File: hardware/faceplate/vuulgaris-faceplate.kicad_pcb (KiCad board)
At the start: 4 copper layers, 298.3 x 137.8 mm, 54 parts, among them J1 HX JN2.54-2x5P TP H8.9, U1 MSP430FR2675TPT, Y1 32.768kHz FC-135 12.5pF

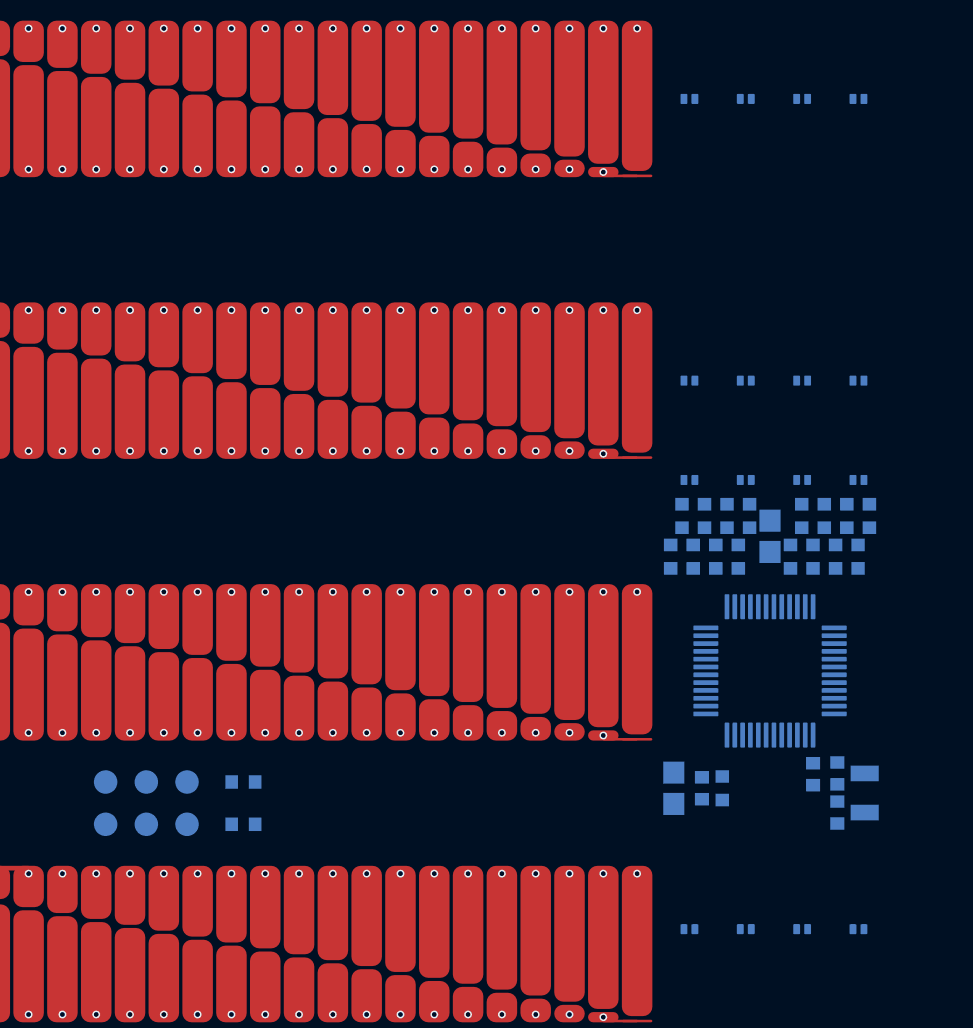
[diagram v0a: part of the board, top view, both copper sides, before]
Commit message: faceplate: networks as a 4x4 grid, silk that does not collide
Dylan: the resistor block did not look good. It was two rows interleaved
at 0.72mm, so the silk boxes overlapped, and the TVS rows (RX0-RX3 per
pad) did not match the R order (block-major), so the ratsnest crossed.

Now one column per CapTIvate block, standing over its own pins, and one
row per pad. Each cell is the TVS directly on its 470R, pin 1 over pin 1
(ADR 0004 already puts both by the MCU; what counts is the order and a
short ground). Traces run down the left of every column: worked through
both corners, that order reaches pins 23-39 with no crossing, so every
TVS grounds to its right and all 16 cells are the same. C3 sits in the
wider middle channel over pin 31.

Pitches from the silk, not the library's undersized courtyards: rows 4.0,
columns 3.2 / 4.5 / 3.2. The crystal group respaced (C2 across the corner
by pins 1/48, C5/C6 lying beside Y1's pads); test pads in one row with
signal labels on silk, per the main board's rule; 470R references on end
beside each part, TVS and TP references on B.Fab. Silk overlaps 61 -> 0;
the 31 silk-over-copper left are the library's pin-1 dots, as on the
main board.

Checked: mksch/netcheck 145/145; boardcheck parity 0, clearance 0; DRC
--unrouted 0 errors; panelcheck 10 OK, 1 TODO (OLED window).
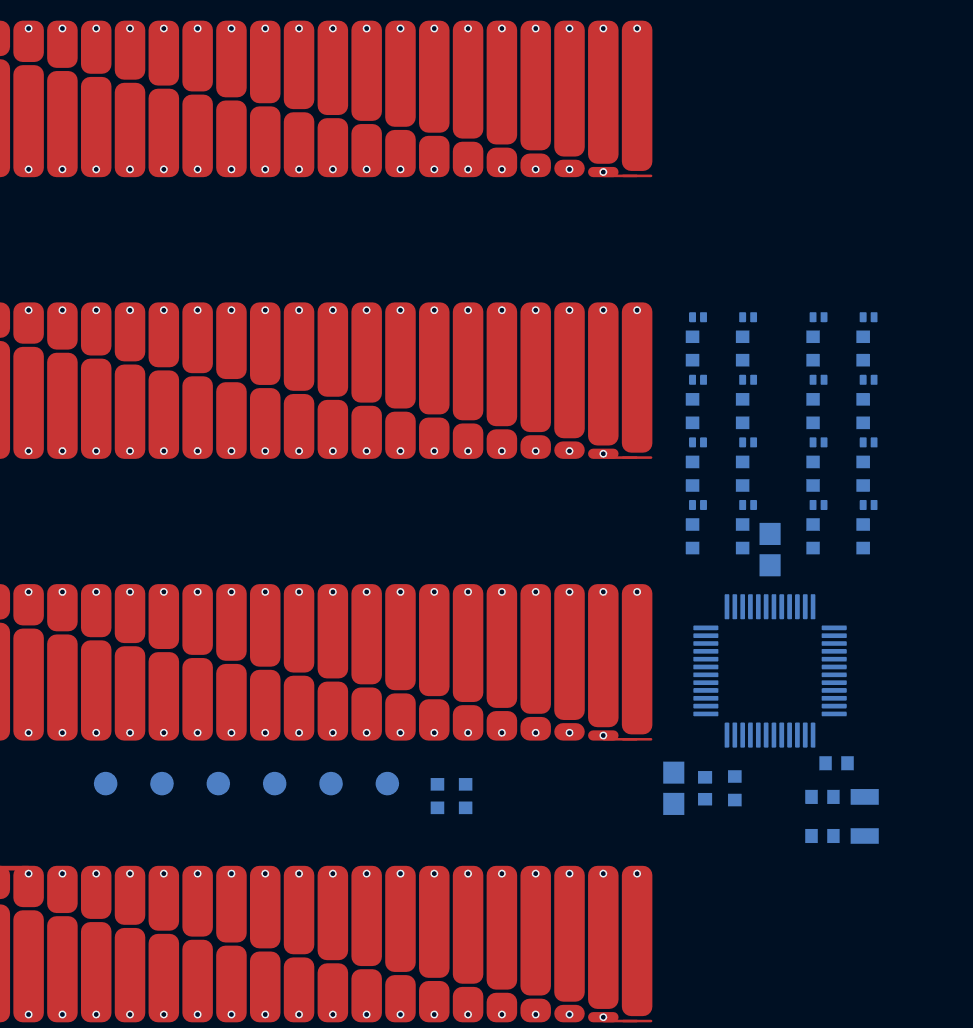
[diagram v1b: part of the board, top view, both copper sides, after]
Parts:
- moved D43 27.1 mm to (387.6, 143.4)
- moved D44 27.1 mm to (390.8, 143.4)
- moved D41 27.1 mm to (379.9, 143.4)
- moved D42 27.1 mm to (383.1, 143.4)
- moved R3 14.3 mm to (365.0, 162.0), turned to -90 degrees
- moved D13 14.0 mm to (387.6, 131.4)
- moved D14 14.0 mm to (390.8, 131.4)
- moved D11 14.0 mm to (379.9, 131.4)
- moved D12 13.9 mm to (383.1, 131.4)
- moved R14 13.4 mm to (390.4, 133.4)
- moved R12 13.4 mm to (382.7, 133.4)
- moved R13 13.4 mm to (387.2, 133.4)
- moved R11 13.4 mm to (379.5, 133.4)
- moved TP6 13.1 mm to (360.0, 161.2)
- moved R2 12.4 mm to (363.2, 162.0), turned to -90 degrees
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
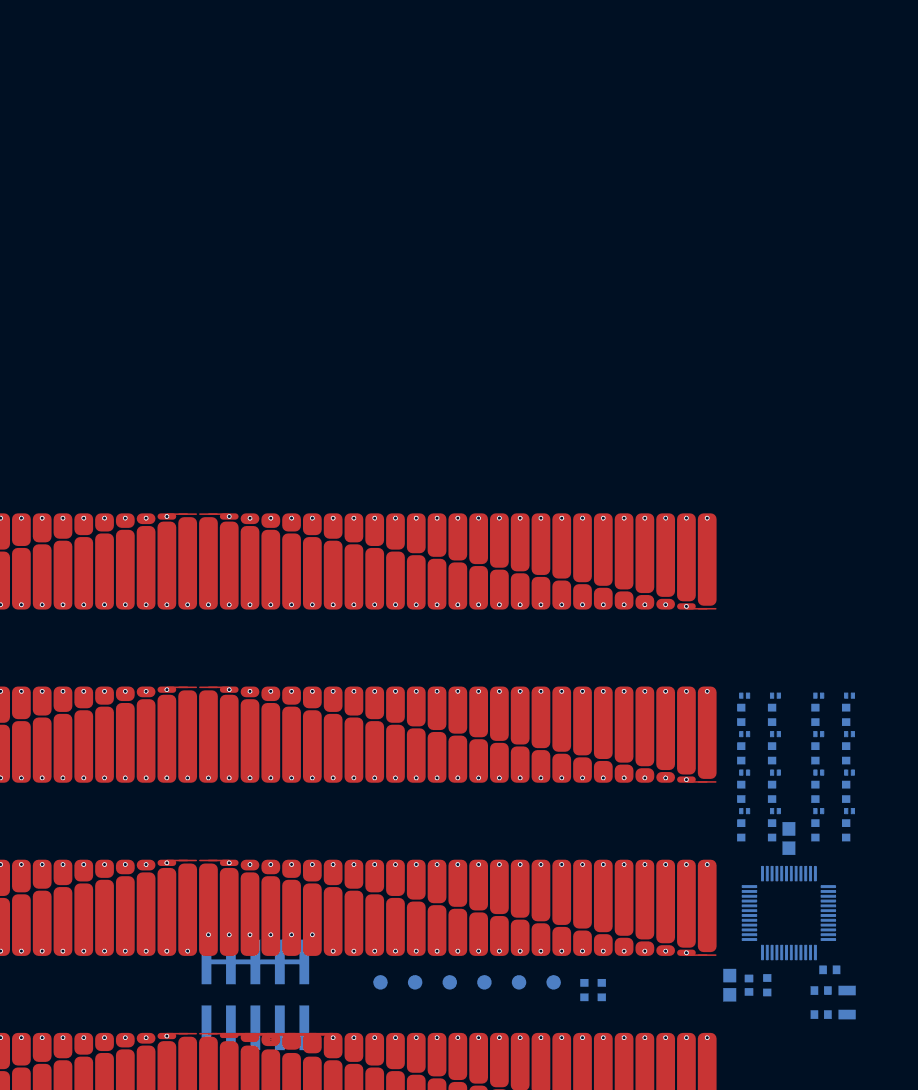
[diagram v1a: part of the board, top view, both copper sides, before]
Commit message: faceplate: OLED window; a wall check that caught parts on the wall top
The window is derived, not drawn: the generator's oled_window() takes the
DS1 position it already emits, the HS242L01 drawing (PCB 72 x 43 -- the
spec table's "68 x 43" is the hole pitch -- AA 55.01 x 27.49 centred
along the long axis, 5.11 below the top edge and 10.4 above the bottom)
and the stack-up. The lift is not chosen (3-5mm), so it is sized at the
deepest: face 4.4mm under the outer surface. 60.09 x 33.90, r 1.0: the
whole active area in view at 45 deg from the player's side, 30 from the
sides, 25 from the back, and never within 1mm of the glass edge, so only
black glass shows past the pixels. It is lopsided because the glass's
wide black band is on the player's side. The panel art draws the window
in place of the old 70 x 42 stand-in box. No chamfer: JLC cannot bevel
an internal cutout.

mkholes.py draws it on Edge.Cuts; panelcheck checks it against the
generator, and the generator's module centre against the main board's
four DS1 holes (both watched failing on a 0.2mm plant). panelcheck
--strict: 13 OK, 0 TODO.

Also a new panelcheck row: every back-side part inside the enclosure
walls, where the faceplate rests on the wall tops. It caught Dylan's
Pcbnew adjustments (grid +1.25/-0.25, corner group lowered, saved 03:43)
putting D14/D24/D34/D44 and Y1 0.56-0.64mm onto the wall; it passes on
the previous commit. Kept his moves, brought RX3's column in 0.73 (its
channel stays 1.47mm, room for three traces), Y1 in 0.85, and C3 back
0.5 -- centred, it left RX2's traces 1.14mm past R43 and put R43's label
on its silk. mkplace.py now records these positions; re-run against his
saved board, only those ten parts differ.

Checked: generator --check all pass, placement file unchanged;
mksch/netcheck 145/145; boardcheck parity 0, clearance 0; DRC --unrouted
0 errors, 0 silk overlaps; panelcheck --strict 13 OK; main board DRC 0
errors, place.py all 24.
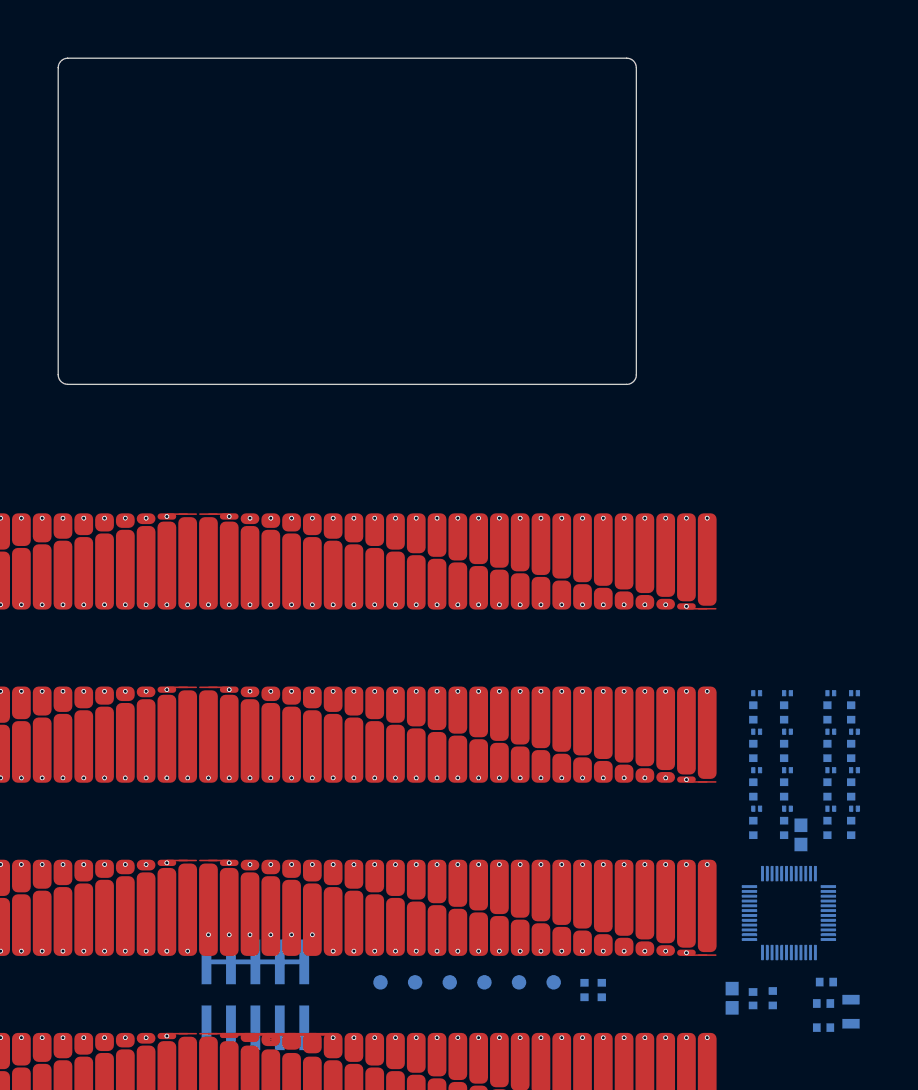
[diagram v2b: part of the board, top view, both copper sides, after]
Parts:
- moved R1 1.47 mm to (382.8, 162.8)
- moved C4 1.46 mm to (380.7, 162.9)
- moved C1 1.37 mm to (378.6, 162.8)
- moved C5 1.37 mm to (388.1, 163.4)
- moved C6 1.37 mm to (388.1, 165.9)
- moved C2 1.32 mm to (388.4, 161.2)
- moved C3 1.31 mm to (385.7, 145.9)
- moved D11 1.27 mm to (381.1, 131.2)
- moved D12 1.27 mm to (384.3, 131.2)
- moved D13 1.27 mm to (388.8, 131.2)
- moved D21 1.27 mm to (381.1, 135.2)
- moved D22 1.27 mm to (384.3, 135.2)
- moved D23 1.27 mm to (388.8, 135.2)
- moved D31 1.27 mm to (381.1, 139.2)
- moved D32 1.27 mm to (384.3, 139.2)
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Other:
- outline, holes or cut-outs redrawn
